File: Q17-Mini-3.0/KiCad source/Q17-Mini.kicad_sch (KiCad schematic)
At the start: 80 parts, among them J1 INPUT, J2-1 SPK+, J2-2 SPK-, J3-1 V+, J3-2 GND, J3-3 V-, Q1 IRF610, Q10 KSA992, Q12 KSC1845, Q13 IRF610, Q14 IRF9610, Q15 FQA46N15, Q16 IXTH48P20P, Q2 KSA992, Q3 KSC1845, Q4 IRF9610, Q5 FQPF7P20, Q6 2SK3564, Q7 LSK170B, Q8 DN2540, Q9 BS250P, U1 OPA1611, U2 NDC7003P

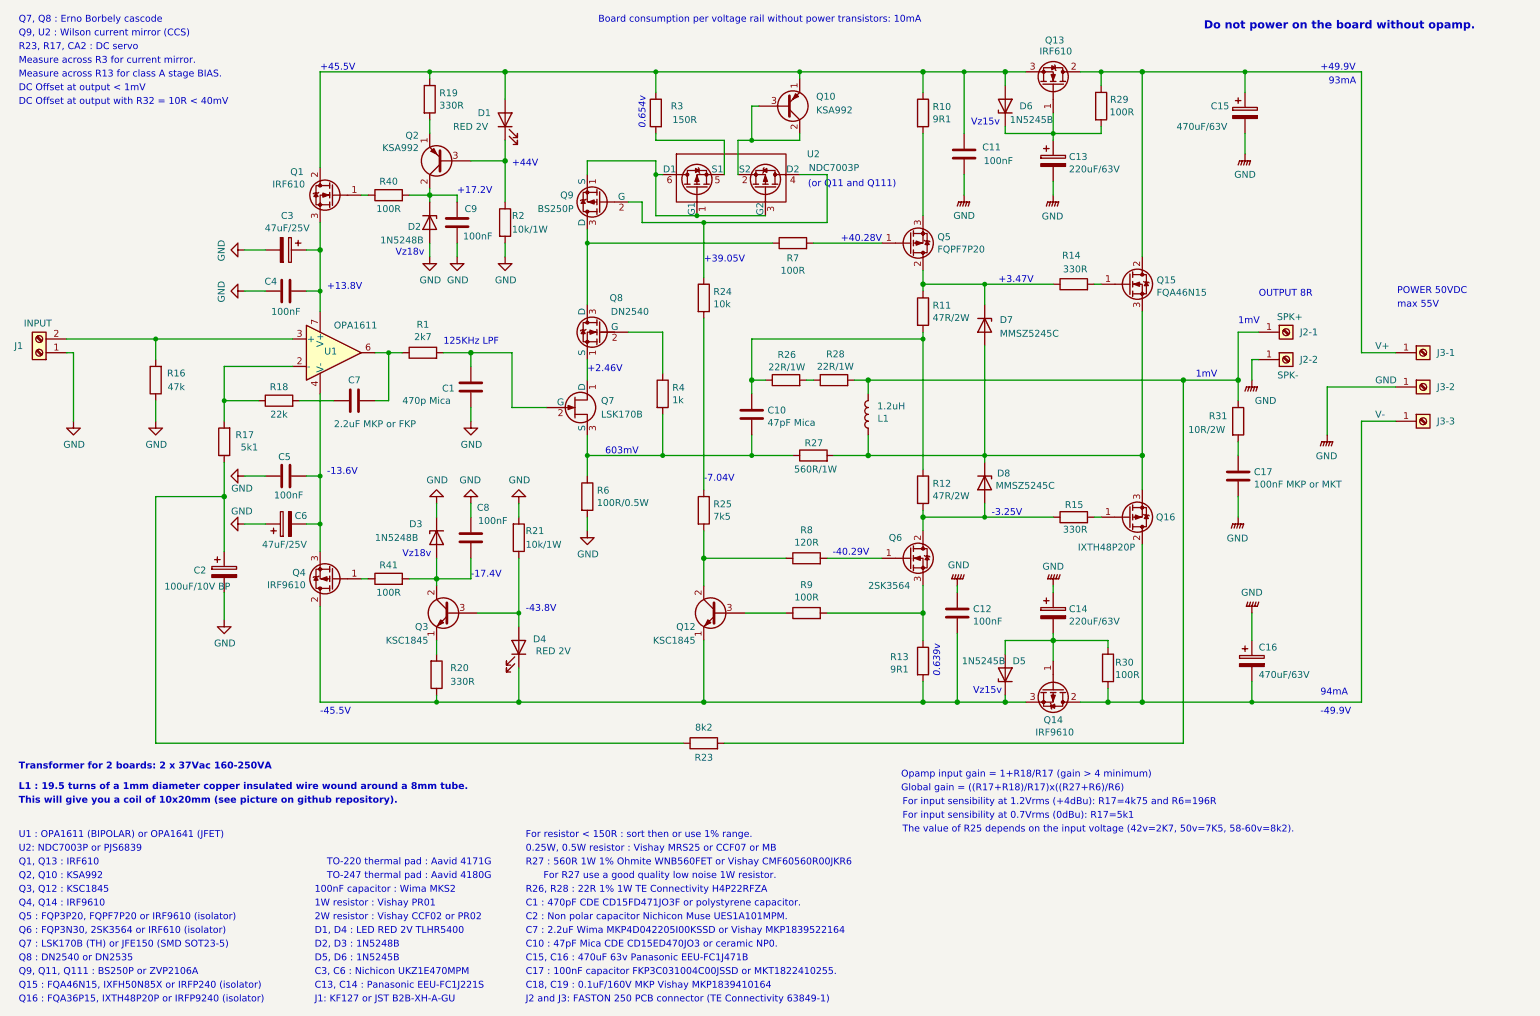
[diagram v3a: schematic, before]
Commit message: Update Q17-MIni diagram (R15=150R)
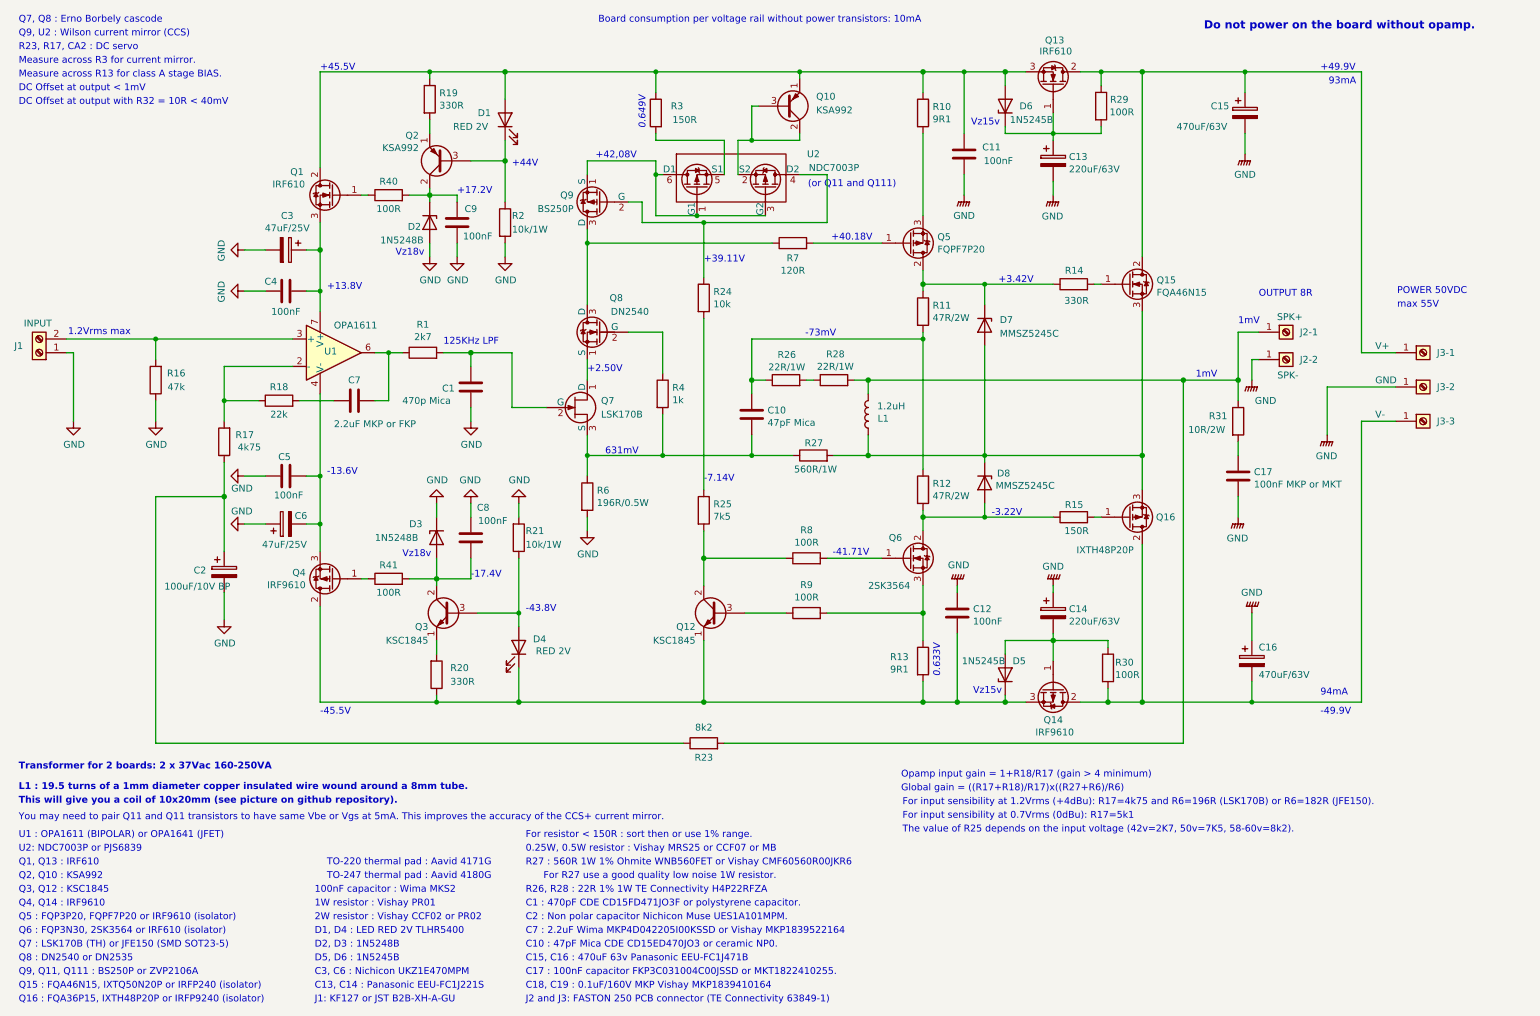
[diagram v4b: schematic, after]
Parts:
- C15, C16: footprint Capacitor_THT:CP_Radial_D18.0mm_P7.50mm -> Capacitor_THT:CP_Radial_D16.0mm_P7.50mm
- R15: value 330R -> 150R; Mouser 594-MRS25000C3300FCT -> 594-MRS25000C1500FRP; Part# MRS25000C3300FCT00 -> MRS25000C1500FRP00
- R17: value 5k1 -> 4k75; Mouser 594-MRS25000C5101FRP -> 594-MRS25000C4751FRP; Part# MRS25000C5101FRP00 -> MRS25000C4751FRP00
- R6: value 100R/0.5W -> 196R/0.5W; Mouser 594-MRS25000C1000FCT -> 594-MRS25000C1960FCT; Part# MRS25000C1000FC100 -> MRS25000C1960FCT00
- R7: value 100R -> 120R
- R8: value 120R -> 100R
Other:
- note added: "+2.50V"
- note added: "+3.42V"
- note added: "+39.11V"
- note added: "+40.18V"
- note added: "+42,08V"
- note added: "-3.22V"
- note added: "-41.71V"
- note added: "-7.14V"
- note added: "-73mV"
- note added: "0.633V"
- note added: "0.649V"
- note added: "1.2Vrms max"
- note added: "631mV"
- note added: "For input sensibility at 1.2Vrms (+4dBu): R17=4k75 and R6=196R (LSK170B) or R6=182R (JFE150)."
- note added: "Q15 : FQA46N15, IXTQ50N20P or IRFP240 (isolator)"
- note added: "You may need to pair Q11 and Q11 transistors to have same Vbe or Vgs at 5mA. This improves the accuracy of the CCS+ current mirror."
- note removed: "+2.46V"
- note removed: "+3.47V"
- note removed: "+39.05V"
- note removed: "+40.28V"
- note removed: "-3.25V"
- note removed: "-40.29V"
- note removed: "-7.04V"
- note removed: "0.639v"
- note removed: "0.654v"
- note removed: "603mV"
- note removed: "For input sensibility at 1.2Vrms (+4dBu): R17=4k75 and R6=196R"
- note removed: "Q15 : FQA46N15, IXFH50N85X or IRFP240 (isolator)"
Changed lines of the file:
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@@
 	(title_block
 		(title "Q17-Mini Amplifier")
-		(date "2024-07-15")
+		(date "2024-07-27")
 		(rev "2.3.3")
 		(company "Principe circuit by Tiberiu Vicol")
@@
 		)
 	)
-	(text "Q15 : FQA46N15, IXFH50N85X or IRFP240 (isolator)"
+	(text "Q15 : FQA46N15, IXTQ50N20P or IRFP240 (isolator)"
 		(exclude_from_sim no)
 		(at 13.97 194.31 0)
@@
 		)
 	)
-	(text "+2.46V"
+	(text "+2.50V"
 		(exclude_from_sim no)
 		(at 119.38 80.01 0)
@@
 		)
 	)
+	(text "You may need to pair Q11 and Q11 transistors to have same Vbe or Vgs at 5mA. This improves the accuracy of the CCS+ current mirror.\n"
+		(exclude_from_sim no)
+		(at 13.97 163.068 0)
+		(effects
+			(font
+				(size 1.27 1.27)
+			)
+			(justify left bottom)
+		)
+	)
 	(text "-49.9V"
 		(exclude_from_sim no)
@@
 		)
 	)
-	(text "-3.25V"
+	(text "-3.22V"
 		(exclude_from_sim no)
 		(at 194.31 106.68 0)
@@
 		)
 	)
-	(text "For input sensibility at 1.2Vrms (+4dBu): R17=4k75 and R6=196R"
+	(text "For input sensibility at 1.2Vrms (+4dBu): R17=4k75 and R6=196R (LSK170B) or R6=182R (JFE150)."
 		(exclude_from_sim no)
 		(at 177.8 160.274 0)
@@
 		)
 	)
-	(text "603mV"
+	(text "631mV"
 		(exclude_from_sim no)
 		(at 122.682 95.25 0)
@@
 		)
 	)
+	(text "1.2Vrms max"
+		(exclude_from_sim no)
+		(at 23.114 73.152 0)
+		(effects
+			(font
+				(size 1.27 1.27)
+			)
+			(justify left bottom)
+		)
+	)
 	(text "U1 : OPA1611 (BIPOLAR) or OPA1641 (JFET)"
 		(exclude_from_sim no)
@@
 		)
 	)
-	(text "-7.04V"
+	(text "-7.14V"
 		(exclude_from_sim no)
 		(at 140.97 100.33 0)
@@
 		)
 	)
-	(text "+3.47V"
+	(text "+3.42V"
 		(exclude_from_sim no)
 		(at 195.58 63.5 0)
@@
 		)
 	)
-	(text "0.654v"
+	(text "0.649V"
 		(exclude_from_sim no)
 		(at 130.302 34.798 90)
@@
 		)
 	)
-	(text "+40.28V"
+	(text "+40.18V"
 		(exclude_from_sim no)
-		(at 166.37 55.88 0)
+		(at 164.592 55.626 0)
 		(effects
 			(font
@@
 		)
 	)
+	(text "+42,08V"
+		(exclude_from_sim no)
+		(at 120.904 40.386 0)
+		(effects
+			(font
+				(size 1.27 1.27)
+				(color 255 3 20 1)
+			)
+			(justify left bottom)
+		)
+	)
 	(text "+44V"
 		(exclude_from_sim no)
@@
 		)
 	)
-	(text "-40.29V"
+	(text "-41.71V"
 		(exclude_from_sim no)
 		(at 164.846 114.046 0)
@@
 		)
 	)
+	(text "-73mV"
+		(exclude_from_sim no)
+		(at 159.766 73.406 0)
+		(effects
+			(font
+				(size 1.27 1.27)
+				(color 255 3 20 1)
+			)
+			(justify left bottom)
+		)
+	)
 	(text "Measure across R3 for current mirror."
 		(exclude_from_sim no)
@@
 		)
 	)
-	(text "0.639v"
+	(text "0.633V"
 		(exclude_from_sim no)
 		(at 184.912 136.398 90)
@@
 		)
 	)
-	(text "+39.05V"
+	(text "+39.11V"
 		(exclude_from_sim no)
 		(at 140.97 59.69 0)
@@
 			)
 		)
-		(property "Footprint" "Capacitor_THT:CP_Radial_D18.0mm_P7.50mm"
+		(property "Footprint" "Capacitor_THT:CP_Radial_D16.0mm_P7.50mm"
 			(at 243.5352 137.16 0)
 			(effects
@@
 			)
 		)
-		(property "Value" "330R"
-			(at 212.09 108.966 90)
+		(property "Value" "150R"
+			(at 212.344 109.22 90)
 			(effects
 				(font
@@
 			)
 		)
-		(property "Part#" "MRS25000C3300FCT00"
+		(property "Part#" "MRS25000C1500FRP00"
 			(at 209.55 106.68 90)
 			(effects
@@
 			)
 		)
-		(property "Mouser" "594-MRS25000C3300FCT"
+		(property "Mouser" "594-MRS25000C1500FRP"
 			(at 209.55 106.68 90)
 			(effects
@@
 		(dnp no)
 		(property "Reference" "R14"
-			(at 210.82 58.166 90)
+			(at 211.328 60.96 90)
 			(effects
 				(font
@@
 		)
 		(property "Value" "330R"
-			(at 212.09 60.706 90)
+			(at 212.344 66.548 90)
 			(effects
 				(font
@@
 			)
 		)
-		(property "Value" "100R"
+		(property "Value" "120R"
 			(at 157.48 60.96 90)
 			(effects
@@
 			)
 		)
-		(property "Footprint" "Capacitor_THT:CP_Radial_D18.0mm_P7.50mm"
+		(property "Footprint" "Capacitor_THT:CP_Radial_D16.0mm_P7.50mm"
 			(at 242.2652 35.56 0)
 			(effects
@@
 			)
 		)
-		(property "Value" "120R"
+		(property "Value" "100R"
 			(at 160.02 111.3725 90)
 			(effects
@@
 			)
 		)
-		(property "Value" "5k1"
+		(property "Value" "4k75"
 			(at 56.7302 93.7195 0)
 			(effects
@@
 			)
 		)
-		(property "Description" "5k1 resistor"
+		(property "Description" ""
 			(at 52.07 92.71 0)
 			(effects
@@
 			)
 		)
-		(property "Part#" "MRS25000C5101FRP00"
+		(property "Part#" "MRS25000C4751FRP00"
 			(at 52.07 92.71 0)
 			(effects
@@
 			)
 		)
-		(property "Mouser" "594-MRS25000C5101FRP"
+		(property "Mouser" "594-MRS25000C4751FRP"
 			(at 52.07 92.71 0)
 			(effects
@@
 			)
 		)
-		(property "Value" "100R/0.5W"
+		(property "Value" "196R/0.5W"
 			(at 121.158 104.019 0)
 			(effects
@@
 			)
 		)
-		(property "Part#" "MRS25000C1000FC100"
+		(property "Part#" "MRS25000C1960FCT00"
 			(at 119.38 102.87 0)
 			(effects
@@
 			)
 		)
-		(property "Mouser" "594-MRS25000C1000FCT"
+		(property "Mouser" "594-MRS25000C1960FCT"
 			(at 119.38 102.87 0)
 			(effects
@@
 		)
 		(property "Value" "IXTH48P20P"
-			(at 210.312 112.268 0)
+			(at 210.058 112.776 0)
 			(effects
 				(font
@@
 			)
 		)
-		(property "Datasheet" "https://www.mouser.fr/datasheet/2/240/ixyss09010_1-2272779.pdf"
+		(property "Datasheet" "https://www.mouser.fr/datasheet/2/240/media-3323106.pdf"
 			(at 219.71 106.68 0)
 			(effects

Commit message: Update Q17-Mini diagram
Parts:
- R7: Mouser 594-MRS25000C1000FCT -> 594-MRS25000C1200FCT; Part# MRS25000C1000FCT00 -> MRS25000C1200FCT00
- R8: Mouser 594-MRS25000C1200FCT -> 594-MRS25000C1000FCT; Part# MRS25000C1200FCT00 -> MRS25000C1000FCT00
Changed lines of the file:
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@@
 	(title_block
 		(title "Q17-Mini Amplifier")
-		(date "2024-07-27")
+		(date "2024-07-28")
 		(rev "2.3.3")
 		(company "Principe circuit by Tiberiu Vicol")
@@
 			)
 		)
-		(property "Part#" "MRS25000C1000FCT00"
+		(property "Part#" "MRS25000C1200FCT00"
 			(at 157.48 55.88 90)
 			(effects
@@
 			)
 		)
-		(property "Mouser" "594-MRS25000C1000FCT"
+		(property "Mouser" "594-MRS25000C1200FCT"
 			(at 157.48 55.88 90)
 			(effects
@@
 			)
 		)
-		(property "Part#" "MRS25000C1200FCT00"
+		(property "Part#" "MRS25000C1000FCT00"
 			(at 160.02 114.3 90)
 			(effects
@@
 			)
 		)
-		(property "Mouser" "594-MRS25000C1200FCT"
+		(property "Mouser" "594-MRS25000C1000FCT"
 			(at 160.02 114.3 90)
 			(effects

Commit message: Upload Q17-Mini 3.0.2
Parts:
- added D8, D9: SL1M-AQ, Diode_SMD:D_SOD-123, symbol Diode:US1B
- C15, C16: Mouser 594-MAL204858222E3 -> 667-EEU-FC1J471B; Part# MAL204858222E3 -> EEU-FC1J471B
- C3, C6: Mouser 647-UKZ1E470MPM -> 647-UKW2A470MPD; Part# Nichicon Muse UKZ1E470MPM -> UKW2A470MPD
- Q16: value IXTH48P20P -> IXTQ36P15P
- R10, R13: value 9R1 -> 8R2; Mouser 594-MBB02070C9108FCT -> 594-MRS25000C8208FCT; Part# MBB02070C9108FCT00 -> MRS25000C8208FCT00
- R15: value 150R -> 330R; Mouser 594-MRS25000C1500FRP -> 594-MRS25000C3300FCT; Part# MRS25000C1500FRP00 -> MRS25000C3300FCT00
- R7: value 120R -> 100R; Mouser 594-MRS25000C1200FCT -> 594-MRS25000C1000FCT; Part# MRS25000C1200FCT00 -> MRS25000C1000FCT00
- R8: Part# MRS25000C1000FCT00 -> MRS25000C1000FCT
- renumbered D8 to D10
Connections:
- net at L1.1, Q15.3 (S), Q16.3 (S)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: now also D8.1 (K), D9.2 (A); no longer D10.1 (K), D7.2 (A)
- new net: D7.2 (A), D8.2 (A)
- new net: D10.1 (K), D9.1 (K)
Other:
- note added: "(or JFE150)"
- note added: "(or Q11 / Q111)"
- note added: "+13.78V"
- note added: "+17V"
- note added: "+3.58V"
- note added: "+38.78V"
- note added: "+40,36V"
- note added: "+42,09V"
- note added: "+45.8V"
- note added: "+50V"
- note added: "-11mV"
- note added: "-14V"
- note added: "-17.2V"
- note added: "-3.61V"
- note added: "-43.95V"
- note added: "-45.7V"
- note added: "-50V"
- note added: "-7.20V"
- note added: "101mA"
- note added: "452mV"
- note added: "627mV"
- note added: "633mV"
- note added: "647mV"
- note added: "98mA"
- note added: "For input sensibility at 0.7Vrms (0dBu): R17=5k1 and R6=100R"
- note added: "Measurements taken from warm card (15mm)."
- note added: "Q15 : FQA46N15 or IXTQ36N30P (isolator)"
- note added: "Q16 : FQA36P15 or IXTQ36P15P (isolator)"
- note added: "Q5 : FQP3P20 or FQPF7P20 (isolator)"
- note added: "Q6 : FQP3N30 or 2SK3564 (isolator)"
- note added: "The value of R25 depends on the input voltage (42v=2K7, 50v=7K5, 54-60v=8k2)."
- note added: "Transformer for 2 boards: 2 x 37Vac 160-250VA (clip = 1.7A per rail @ 50V)"
- note added: "U1 : OPA1611 (BIPOLAR) or OPA828 (JFET)"
- note removed: "(or Q11 and Q111)"
- note removed: "+13.8V"
- note removed: "+17.2V"
- note removed: "+3.42V"
- note removed: "+39.11V"
- note removed: "+40.18V"
- note removed: "+42,08V"
- note removed: "+45.5V"
- note removed: "+49.9V"
- note removed: "-13.6V"
- note removed: "-17.4V"
- note removed: "-3.22V"
- note removed: "-43.8V"
- note removed: "-45.5V"
- note removed: "-49.9V"
- note removed: "-7.14V"
- note removed: "-73mV"
- note removed: "0.633V"
- note removed: "0.649V"
- note removed: "1.2Vrms max"
- note removed: "631mV"
- note removed: "93mA"
- note removed: "94mA"
- note removed: "DC Offset at output with R32 = 10R < 40mV"
- note removed: "For input sensibility at 0.7Vrms (0dBu): R17=5k1"
- note removed: "Q15 : FQA46N15, IXTQ50N20P or IRFP240 (isolator)"
- note removed: "Q16 : FQA36P15, IXTH48P20P or IRFP9240 (isolator)"
- note removed: "Q5 : FQP3P20, FQPF7P20 or IRF9610 (isolator)"
- note removed: "Q6 : FQP3N30, 2SK3564 or IRF610 (isolator)"
- note removed: "The value of R25 depends on the input voltage (42v=2K7, 50v=7K5, 58-60v=8k2)."
- note removed: "Transformer for 2 boards: 2 x 37Vac 160-250VA"
- note removed: "U1 : OPA1611 (BIPOLAR) or OPA1641 (JFET)"
- moved on the sheet: C2, D10, D7, Q12, Q16, Q9, R14, R15, R16, R17, R18, R24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

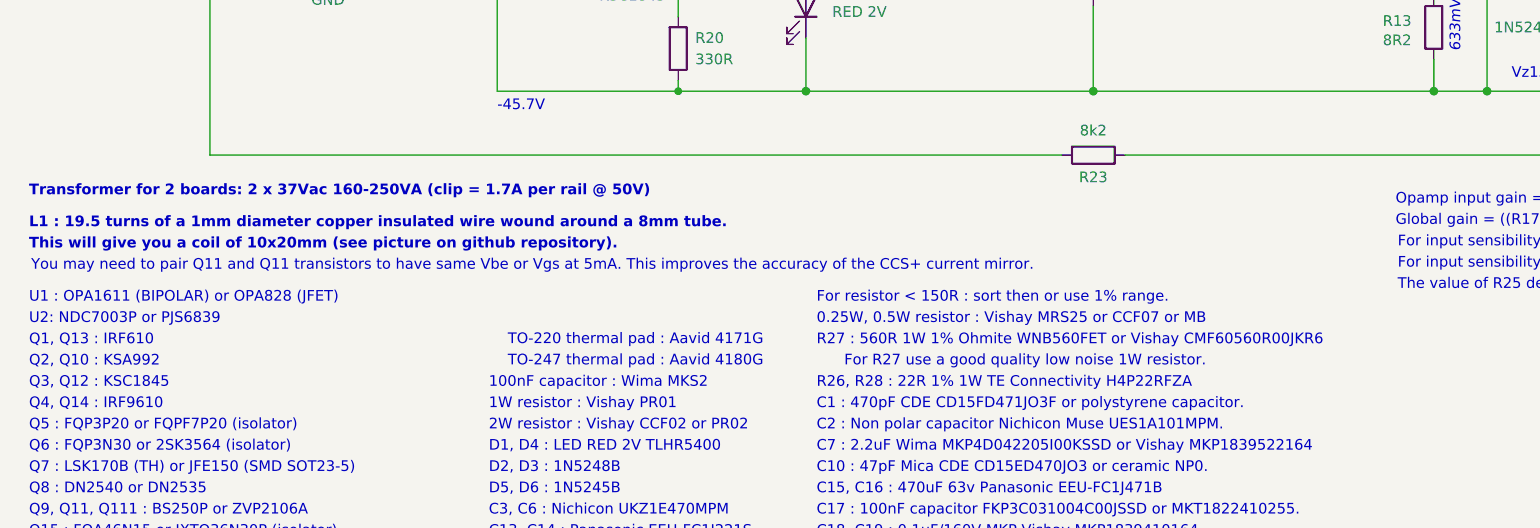
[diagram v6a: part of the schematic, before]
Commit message: Update Q17-Mini-schematic
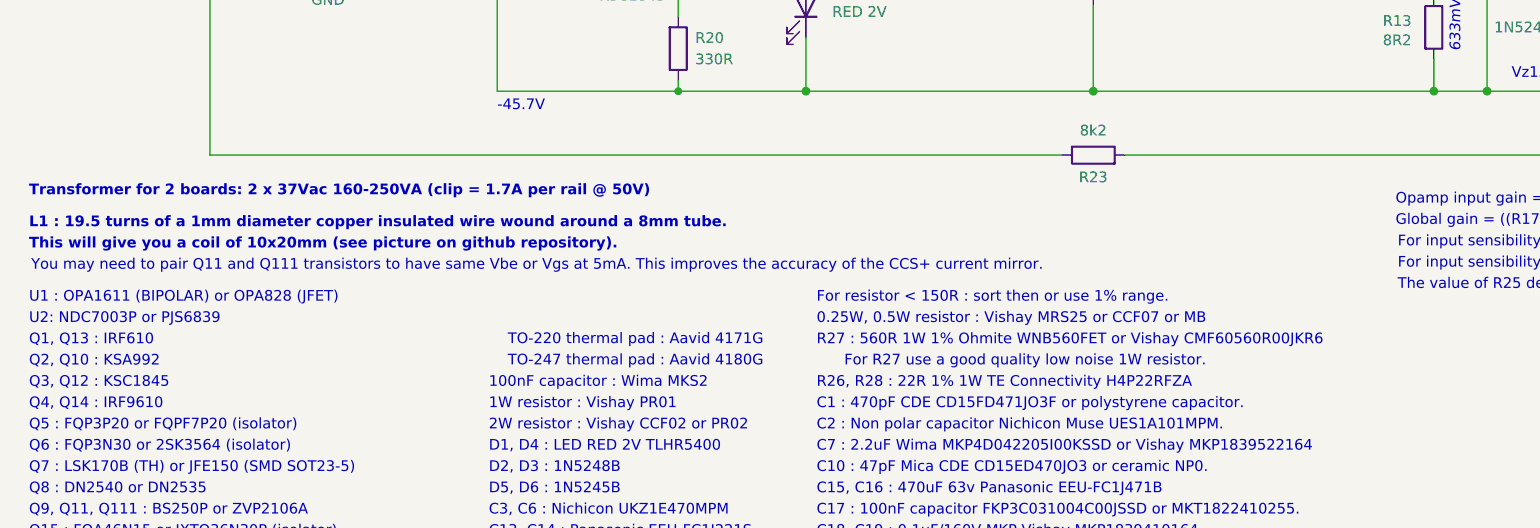
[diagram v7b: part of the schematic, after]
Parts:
- Q16: Mouser 747-IXTH48P20P -> 747-IXTQ36P15P; Part# IXTH48P20P -> IXTQ36P15P
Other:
- note added: "You may need to pair Q11 and Q111 transistors to have same Vbe or Vgs at 5mA. This improves the accuracy of the CCS+ current mirror."
- note removed: "You may need to pair Q11 and Q11 transistors to have same Vbe or Vgs at 5mA. This improves the accuracy of the CCS+ current mirror."
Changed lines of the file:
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@@
 	(title_block
 		(title "Q17-Mini Amplifier")
-		(date "2024-08-23")
+		(date "2024-08-26")
 		(rev "2.3.4")
 		(company "Principe circuit by Tiberiu Vicol")
@@
 		)
 	)
-	(text "You may need to pair Q11 and Q11 transistors to have same Vbe or Vgs at 5mA. This improves the accuracy of the CCS+ current mirror.\n"
+	(text "You may need to pair Q11 and Q111 transistors to have same Vbe or Vgs at 5mA. This improves the accuracy of the CCS+ current mirror.\n"
 		(exclude_from_sim no)
 		(at 14.224 162.56 0)
@@
 			)
 		)
-		(property "Datasheet" "https://www.mouser.fr/datasheet/2/240/ixyss09010_1-2272779.pdf"
+		(property "Datasheet" "https://www.mouser.fr/datasheet/2/240/media-3320788.pdf"
 			(at 219.71 111.76 0)
 			(effects
@@
 			)
 		)
-		(property "Part#" "IXTH48P20P"
+		(property "Part#" "IXTQ36P15P"
 			(at 219.71 111.76 0)
 			(effects
@@
 			)
 		)
-		(property "Mouser" "747-IXTH48P20P"
+		(property "Mouser" "747-IXTQ36P15P"
 			(at 219.71 111.76 0)
 			(effects
